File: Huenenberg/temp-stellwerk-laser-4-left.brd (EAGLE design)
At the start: 99.1 x 61 mm, 120 parts, among them Q1 BSS123, Q10 BSS84, Q11 BSS123, Q12 BSS84, Q13 BSS123, Q14 BSS84, Q15 BSS123, Q16 BSS84, Q17 BSS123, Q18 BSS84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

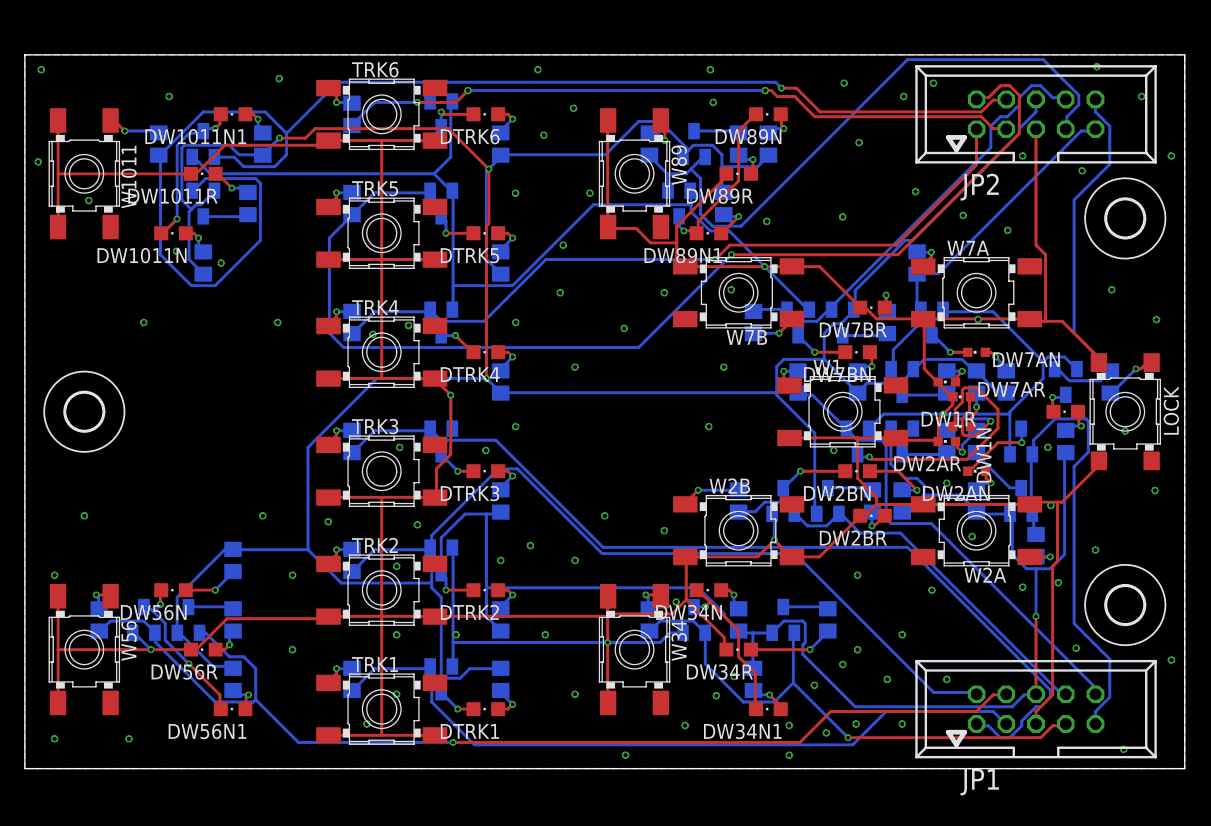
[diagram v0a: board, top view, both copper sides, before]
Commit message: Adds final versions of lasered overlays.
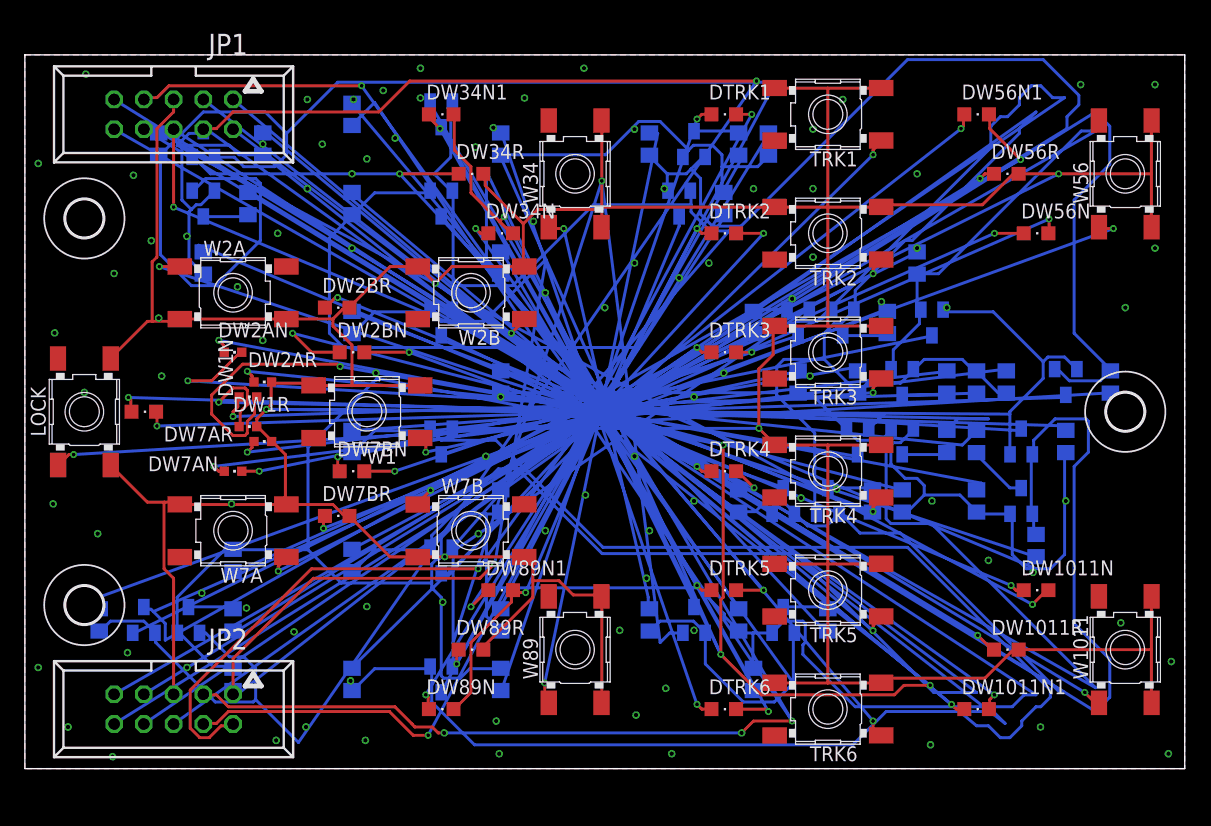
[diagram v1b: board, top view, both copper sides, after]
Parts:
- LOCK: device trainlib:TACTSW-6X6 -> eagleparts:TACTSW-6X6-LASER
- moved W1011 97.7 mm to (94.0, 10.2), turned to 90 degrees
- moved W56 97.7 mm to (94.0, 50.8), turned to 90 degrees
- moved H1 94.8 mm to (5.08, 14.0), turned to 180 degrees
- moved H2 94.8 mm to (5.08, 47.0), turned to 180 degrees
- moved JP1 89.5 mm to (12.7, 55.9), turned to 180 degrees
- moved JP2 89.5 mm to (12.7, 5.08), turned to 180 degrees
- moved H3 88.9 mm to (94.0, 30.5), turned to 180 degrees
- moved LOCK 88.9 mm to (5.08, 30.5), turned to 90 degrees
- moved DW1011N1 81.3 mm to (81.3, 5.08), turned to 270 degrees
- moved DW56N1 81.3 mm to (81.3, 55.9), turned to 270 degrees
- moved DW1011N 79.7 mm to (86.4, 15.2), turned to 270 degrees
- moved DW1011R 79.7 mm to (83.8, 10.2), turned to 270 degrees
- moved DW56N 79.7 mm to (86.4, 45.7), turned to 270 degrees
- moved DW56R 79.7 mm to (83.8, 50.8), turned to 270 degrees
- moved DLOCK 78.7 mm to (10.2, 30.5), turned to 270 degrees
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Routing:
- net +5V: track 396.9 -> 849.9 mm
- net GND: track 538.5 -> 914.2 mm
- net N$32: track 14.0 -> 177.6 mm
- net N$58: track 13.6 -> 172.3 mm
- net CH14: track 59.6 -> 179.9 mm
- net CH2: track 42.0 -> 139.7 mm
- net CH9: track 31.8 -> 129.5 mm
- net CH10: track 29.9 -> 126.4 mm
- net CH1: track 41.5 -> 137.4 mm
- net CH11: track 37.8 -> 132.7 mm
- net CH12: track 55.0 -> 147.3 mm
- net CH3: track 36.0 -> 128.0 mm
- net N$31: track 2.62 -> 94.5 mm
- net N$57: track 4.69 -> 94.4 mm
- net CH6: track 62.8 -> 149.5 mm
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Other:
- board text added: "Fstr-"
- board text added: "festl."
- board text removed: "Fahrstrassen-"
- board text removed: "festlegung"
